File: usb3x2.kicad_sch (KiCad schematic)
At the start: 98 parts

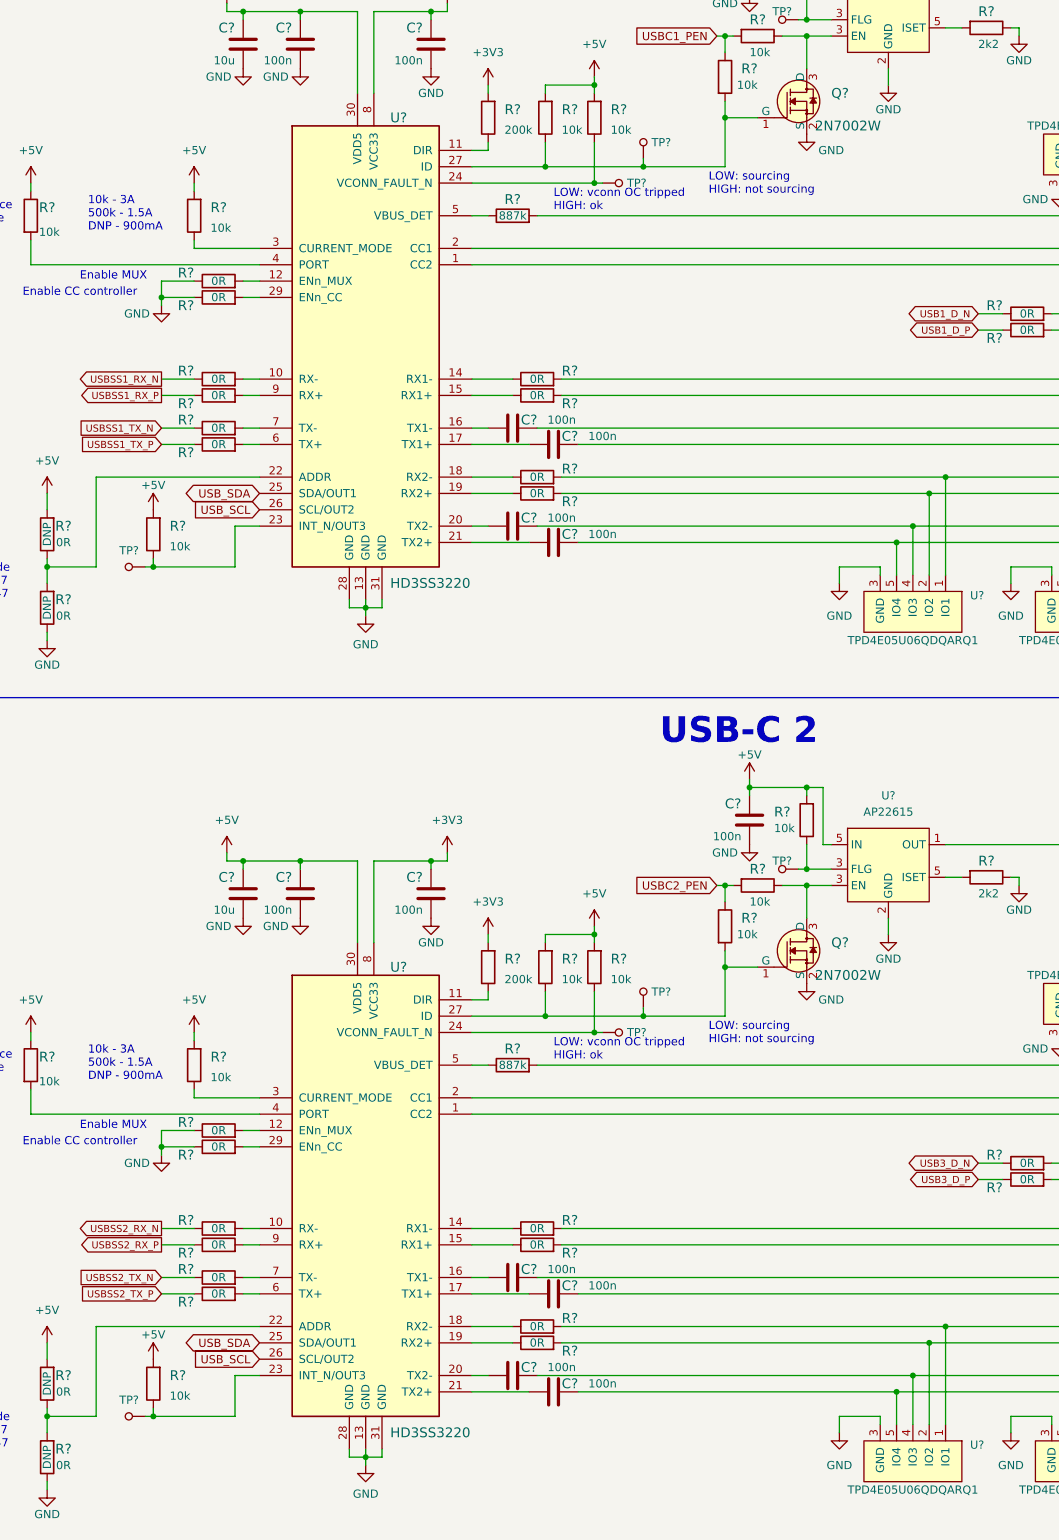
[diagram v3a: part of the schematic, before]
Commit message: Connected gpio signals and 40-pin connector
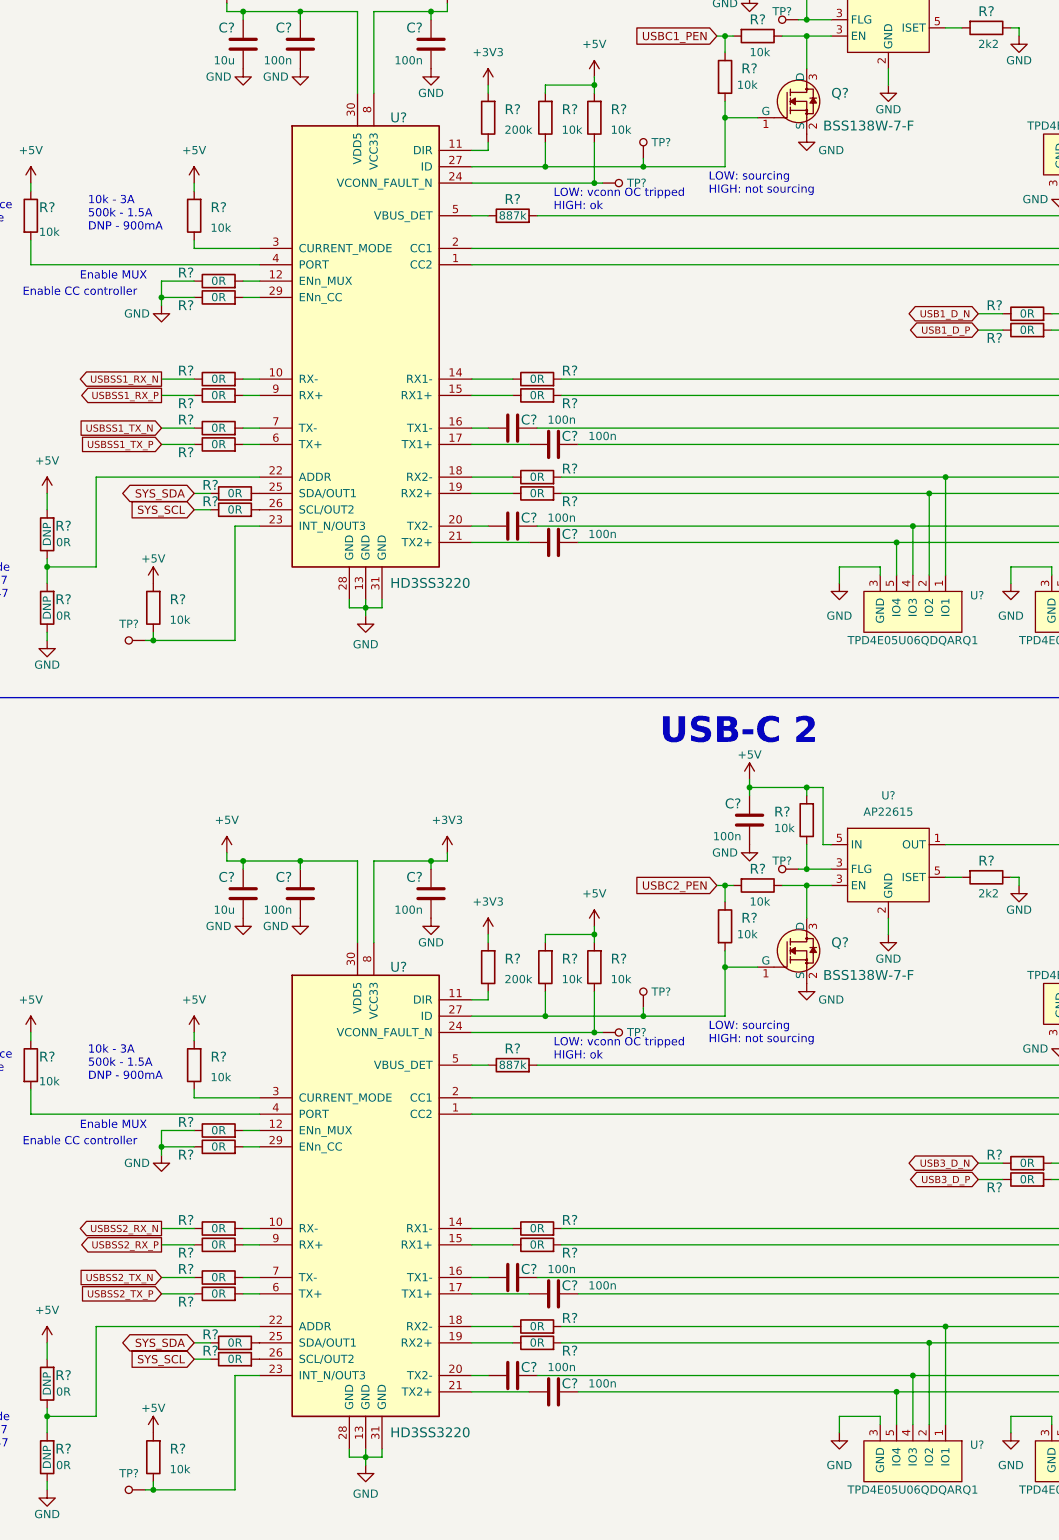
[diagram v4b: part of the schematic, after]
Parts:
- removed Q? (x2): 2N7002W, antmicro-footprints:SOT-323, symbol antmicroTransistorsFETsMOSFETsSingle: 2N7002W
- removed R?: R_10k_0402, antmicro-footprints:0402-res, symbol antmicroResistors0402:R_10k_0402
- removed TP?: TP_SMD_0_75MM, antmicro-footprints:Testpoint_smd_0_75mm, symbol antmicroTestPoints:TP_SMD_0_75MM
- added Q? (x2): BSS138W-7-F, antmicro-footprints:SOT-323, symbol antmicroTransistorsFETsMOSFETsSingle:BSS138W-7-F
- added R? (x4): R_0R_0402, antmicro-footprints:0402-res, symbol antmicroResistors0402:R_0R_0402
- added R?: R_10k_0402, antmicro-footprints:0402-res, symbol antmicroResistors0402:R_10k_0402
- added TP?: TP_SMD_0_75MM, antmicro-footprints:Testpoint_smd_0_75mm, symbol antmicroTestPoints:TP_SMD_0_75MM
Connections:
- net +5V: now also R?.2
- net GND: now also Q?.2 (S), Q?.2 (S)
- net at R?.1, R?.2, TP?.1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: now also Q?.1 (G) (x2)
- net at R?.1, U?.3 (FLG): now also Q?.3 (D) (x2)
- net at U?.23 (INT_N/OUT3): now also R?.1, TP?.1
- net USB_SCL: no longer names the net of U?.26 (SCL/OUT2)
- net USB_SCL: now also R?.2; no longer U?.26 (SCL/OUT2)
- net USB_SDA: no longer names the net of U?.25 (SDA/OUT1)
- net USB_SDA: now also R?.2; no longer U?.25 (SDA/OUT1)
- new net: R?.2, U?.25 (SDA/OUT1)
- new net: R?.2, U?.26 (SCL/OUT2)
- new net SYS_SCL: R?.1, R?.1
- new net SYS_SDA: R?.1, R?.1
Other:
- company: (none) -> Antmicro Ltd
- title: (none) -> USB3 x2
- moved on the sheet: R?, TP?

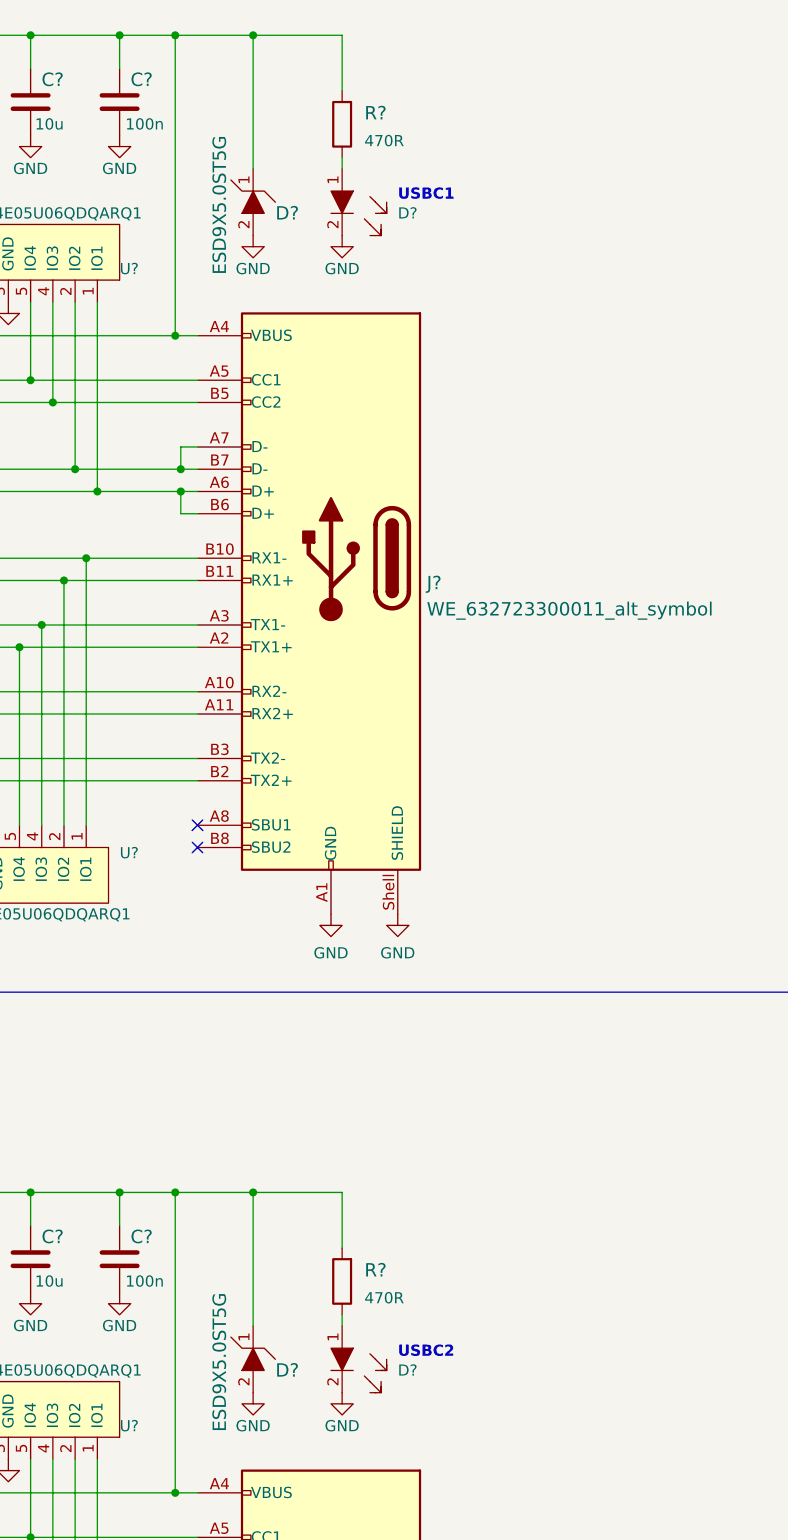
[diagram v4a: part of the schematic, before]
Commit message: Cleaned up schematics, added debug connector, user LEDs and buttons. Connected misc. signals
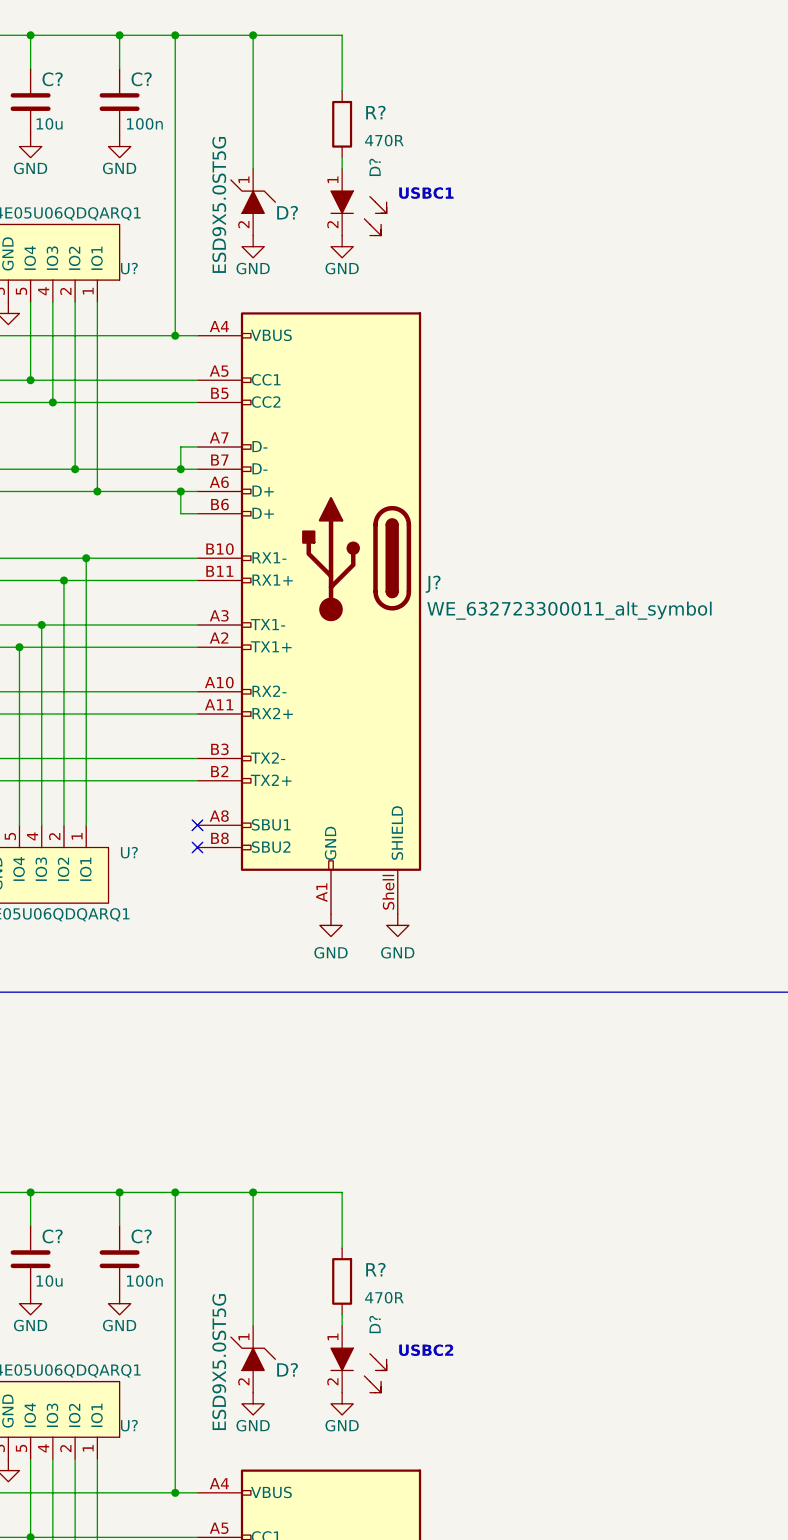
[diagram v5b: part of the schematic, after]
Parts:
- D? (x2): footprint crosslink-nx-video-converter-footprints:LED_0603 -> antmicro-footprints:LED_0603; symbol crosslink-nx-video-converter:LTST-C190GKT -> antmicroLEDIndicationDiscrete:LTST-C190GKT
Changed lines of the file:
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@@
     (pin "2")
   )
-  (symbol (lib_id "crosslink-nx-video-converter:LTST-C190GKT") (at 289.56 59.69 270) (unit 1)
-    (in_bom yes) (on_board yes) (fields_autoplaced)
-    (property "Reference" "D?" (id 0) (at 295.91 59.6899 90)
+  (symbol (lib_id "antmicroLEDIndicationDiscrete:LTST-C190GKT") (at 289.56 59.69 270) (unit 1)
+    (in_bom yes) (on_board yes) (fields_autoplaced)
+    (property "Reference" "D?" (id 0) (at 293.37 53.34 0)
       (effects (font (size 1.27 1.27)) (justify left))
     )
@@
       (effects (font (size 1.524 1.524)) hide)
     )
-    (property "Footprint" "crosslink-nx-video-converter-footprints:LED_0603" (id 2) (at 294.64 64.77 0)
+    (property "Footprint" "antmicro-footprints:LED_0603" (id 2) (at 294.64 64.77 0)
       (effects (font (size 1.524 1.524)) (justify left) hide)
     )
@@
     (pin "2")
   )
-  (symbol (lib_id "crosslink-nx-video-converter:LTST-C190GKT") (at 289.56 191.77 270) (unit 1)
-    (in_bom yes) (on_board yes) (fields_autoplaced)
-    (property "Reference" "D?" (id 0) (at 295.91 191.7699 90)
+  (symbol (lib_id "antmicroLEDIndicationDiscrete:LTST-C190GKT") (at 289.56 191.77 270) (unit 1)
+    (in_bom yes) (on_board yes) (fields_autoplaced)
+    (property "Reference" "D?" (id 0) (at 293.37 185.42 0)
       (effects (font (size 1.27 1.27)) (justify left))
     )
@@
       (effects (font (size 1.524 1.524)) hide)
     )
-    (property "Footprint" "crosslink-nx-video-converter-footprints:LED_0603" (id 2) (at 294.64 196.85 0)
-      (effects (font (size 1.524 1.524)) (justify left) hide)
-    )
+    (property "Footprint" "antmicro-footprints:LED_0603" (id 2) (at 294.64 196.85 0)
+      (effects (font (size 1.524 1.524)) (justify left) hide)
+    )
